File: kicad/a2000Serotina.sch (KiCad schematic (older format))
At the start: 236 parts, among them J1 90121-0766, U1 Teensy++2.0_(C)

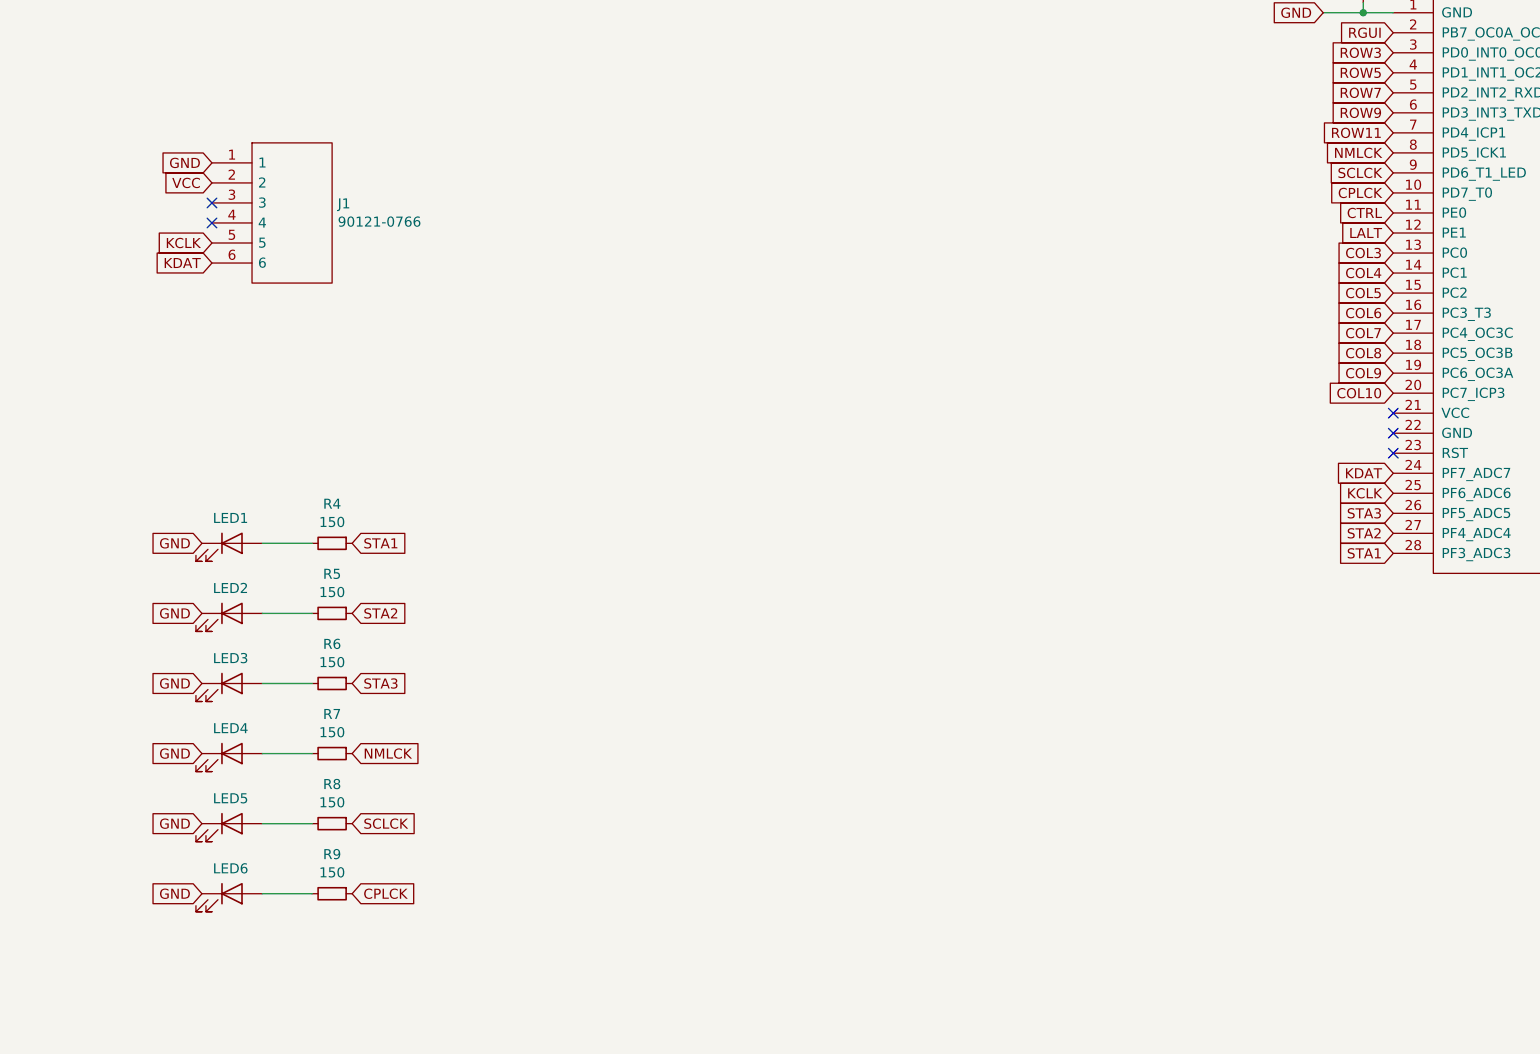
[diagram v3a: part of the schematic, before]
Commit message: Change for V1.4
Now uses a mounting plate from WASD.
1) Adjust dimensions to match WASD PCB
2) Make mounting holes bigger so that PCB sits lower
3) Move resistors so that they are not under plate
4) Move Caps Lock LED to rightmost and move Teensy back to top.
5) J1 moved between Enter + Del
6) Stabilizer holes deleted. Costar Stabilizers now attached to Plate.
7) Minimize hole courtyards to pass Design Rules Check
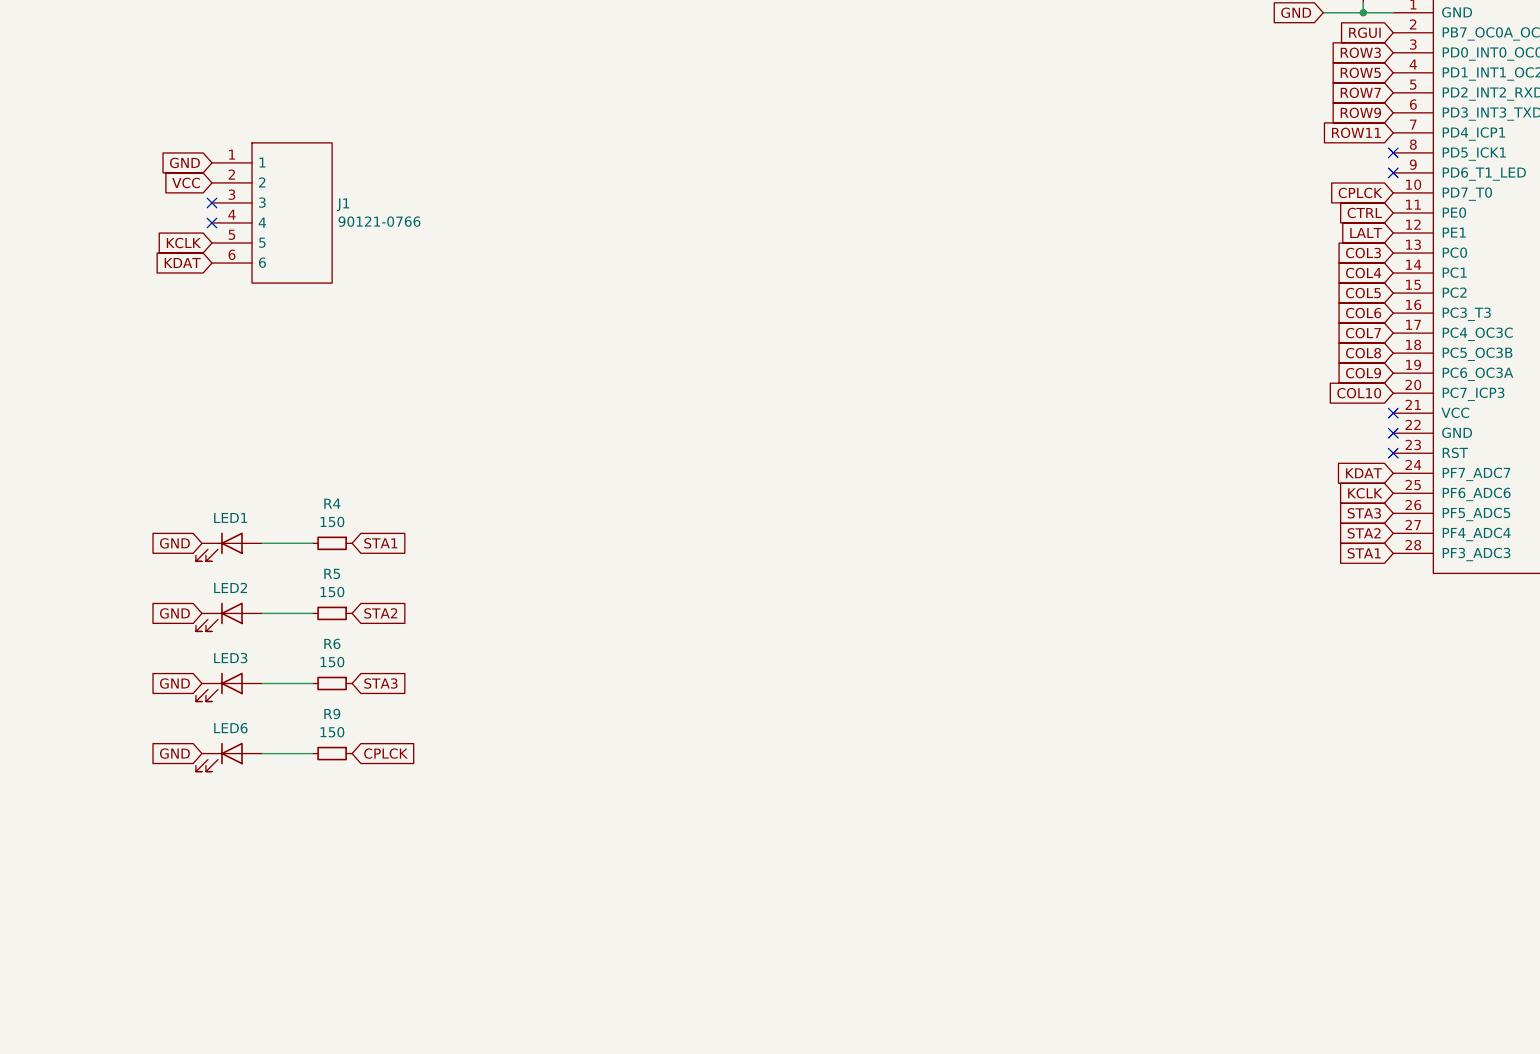
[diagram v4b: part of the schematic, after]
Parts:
- removed LED4, LED5: LED, LED_THT:LED_D3.0mm, symbol Device:LED
- removed R7, R8: 150, Resistor_THT:R_Axial_DIN0207_L6.3mm_D2.5mm_P10.16mm_Horizontal, symbol Device:R_Small
- H1, H2, H3, H4: footprint MountingHole:MountingHole_3.2mm_M3 -> MountingHole:MountingHole_6.4mm_M6
- H5, H6, H7: footprint MountingHole:MountingHole_6.4mm_M6 -> MountingHole:MountingHole_8.4mm_M8
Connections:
- net NMLCK: no longer names the net of U1.8 (PD5_ICK1)
- net SCLCK: no longer names the net of U1.9 (PD6_T1_LED)
- no-connect marks 20 -> 22
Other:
- moved on the sheet: LED6, R9
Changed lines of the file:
@@
 Text GLabel 18300 3800 0    50   Input ~ 0
 COL10
-Text GLabel 18300 2600 0    50   Input ~ 0
-NMLCK
 Text GLabel 18300 2800 0    50   Input ~ 0
 CPLCK
-Text GLabel 18300 2700 0    50   Input ~ 0
-SCLCK
 Text GLabel 18300 4300 0    50   Input ~ 0
 KCLK
@@
 	12650 5250 12900 5250
 $Comp
-L Device:R_Small R7
-U 1 1 60F964C9
-P 13000 5600
-F 0 "R7" V 12804 5600 50  0000 C CNN
-F 1 "150" V 12895 5600 50  0000 C CNN
-F 2 "Resistor_THT:R_Axial_DIN0207_L6.3mm_D2.5mm_P10.16mm_Horizontal" H 13000 5600 50  0001 C CNN
-F 3 "~" H 13000 5600 50  0001 C CNN
-	1    13000 5600
-	0    1    1    0
-$EndComp
-Text GLabel 13100 5600 2    50   Input ~ 0
-NMLCK
-$Comp
-L Device:LED LED4
-U 1 1 60F964D0
-P 12500 5600
-F 0 "LED4" H 12493 5725 50  0000 C CNN
-F 1 "LED" H 12493 5725 50  0001 C CNN
-F 2 "LED_THT:LED_D3.0mm" H 12500 5600 50  0001 C CNN
-F 3 "~" H 12500 5600 50  0001 C CNN
-	1    12500 5600
-	1    0    0    -1
-$EndComp
-Text GLabel 12350 5600 0    50   Input ~ 0
-GND
-Wire Wire Line
-	12650 5600 12900 5600
-$Comp
-L Device:R_Small R8
-U 1 1 60FB4C04
-P 13000 5950
-F 0 "R8" V 12804 5950 50  0000 C CNN
-F 1 "150" V 12895 5950 50  0000 C CNN
-F 2 "Resistor_THT:R_Axial_DIN0207_L6.3mm_D2.5mm_P10.16mm_Horizontal" H 13000 5950 50  0001 C CNN
-F 3 "~" H 13000 5950 50  0001 C CNN
-	1    13000 5950
-	0    1    1    0
-$EndComp
-Text GLabel 13100 5950 2    50   Input ~ 0
-SCLCK
-$Comp
-L Device:LED LED5
-U 1 1 60FB4C0B
-P 12500 5950
-F 0 "LED5" H 12493 6075 50  0000 C CNN
-F 1 "LED" H 12493 6075 50  0001 C CNN
-F 2 "LED_THT:LED_D3.0mm" H 12500 5950 50  0001 C CNN
-F 3 "~" H 12500 5950 50  0001 C CNN
-	1    12500 5950
-	1    0    0    -1
-$EndComp
-Text GLabel 12350 5950 0    50   Input ~ 0
-GND
-Wire Wire Line
-	12650 5950 12900 5950
-$Comp
 L Device:R_Small R10
 U 1 1 610519E9
@@
 F 0 "H1" H 11600 8546 50  0000 L CNN
 F 1 "MountingHole" H 11600 8455 50  0000 L CNN
-F 2 "MountingHole:MountingHole_3.2mm_M3" H 11500 8500 50  0001 C CNN
+F 2 "MountingHole:MountingHole_6.4mm_M6" H 11500 8500 50  0001 C CNN
 F 3 "~" H 11500 8500 50  0001 C CNN
 	1    11500 8500
@@
 F 0 "H2" H 11600 9046 50  0000 L CNN
 F 1 "MountingHole" H 11600 8955 50  0000 L CNN
-F 2 "MountingHole:MountingHole_3.2mm_M3" H 11500 9000 50  0001 C CNN
+F 2 "MountingHole:MountingHole_6.4mm_M6" H 11500 9000 50  0001 C CNN
 F 3 "~" H 11500 9000 50  0001 C CNN
 	1    11500 9000
@@
 F 0 "H3" H 11600 9546 50  0000 L CNN
 F 1 "MountingHole" H 11600 9455 50  0000 L CNN
-F 2 "MountingHole:MountingHole_3.2mm_M3" H 11500 9500 50  0001 C CNN
+F 2 "MountingHole:MountingHole_6.4mm_M6" H 11500 9500 50  0001 C CNN
 F 3 "~" H 11500 9500 50  0001 C CNN
 	1    11500 9500
@@
 F 0 "H4" H 11600 10046 50  0000 L CNN
 F 1 "MountingHole" H 11600 9955 50  0000 L CNN
-F 2 "MountingHole:MountingHole_3.2mm_M3" H 11500 10000 50  0001 C CNN
+F 2 "MountingHole:MountingHole_6.4mm_M6" H 11500 10000 50  0001 C CNN
 F 3 "~" H 11500 10000 50  0001 C CNN
 	1    11500 10000
@@
 F 0 "H5" H 12600 8546 50  0000 L CNN
 F 1 "MountingHole" H 12600 8455 50  0000 L CNN
-F 2 "MountingHole:MountingHole_6.4mm_M6" H 12500 8500 50  0001 C CNN
+F 2 "MountingHole:MountingHole_8.4mm_M8" H 12500 8500 50  0001 C CNN
 F 3 "~" H 12500 8500 50  0001 C CNN
 	1    12500 8500
@@
 F 0 "H6" H 12600 9046 50  0000 L CNN
 F 1 "MountingHole" H 12600 8955 50  0000 L CNN
-F 2 "MountingHole:MountingHole_6.4mm_M6" H 12500 9000 50  0001 C CNN
+F 2 "MountingHole:MountingHole_8.4mm_M8" H 12500 9000 50  0001 C CNN
 F 3 "~" H 12500 9000 50  0001 C CNN
 	1    12500 9000
@@
 F 0 "H7" H 12600 9546 50  0000 L CNN
 F 1 "MountingHole" H 12600 9455 50  0000 L CNN
-F 2 "MountingHole:MountingHole_6.4mm_M6" H 12500 9500 50  0001 C CNN
+F 2 "MountingHole:MountingHole_8.4mm_M8" H 12500 9500 50  0001 C CNN
 F 3 "~" H 12500 9500 50  0001 C CNN
 	1    12500 9500
@@
 Connection ~ 3750 9750
 Wire Wire Line
-	12650 6300 12900 6300
-Text GLabel 12350 6300 0    50   Input ~ 0
+	12650 5600 12900 5600
+Text GLabel 12350 5600 0    50   Input ~ 0
 GND
 $Comp
 L Device:LED LED6
 U 1 1 60FD4854
-P 12500 6300
-F 0 "LED6" H 12493 6425 50  0000 C CNN
-F 1 "LED" H 12493 6425 50  0001 C CNN
-F 2 "LED_THT:LED_D3.0mm" H 12500 6300 50  0001 C CNN
-F 3 "~" H 12500 6300 50  0001 C CNN
-	1    12500 6300
+P 12500 5600
+F 0 "LED6" H 12493 5725 50  0000 C CNN
+F 1 "LED" H 12493 5725 50  0001 C CNN
+F 2 "LED_THT:LED_D3.0mm" H 12500 5600 50  0001 C CNN
+F 3 "~" H 12500 5600 50  0001 C CNN
+	1    12500 5600
 	1    0    0    -1
 $EndComp
-Text GLabel 13100 6300 2    50   Input ~ 0
+Text GLabel 13100 5600 2    50   Input ~ 0
 CPLCK
 $Comp
 L Device:R_Small R9
 U 1 1 60FD484D
-P 13000 6300
-F 0 "R9" V 12804 6300 50  0000 C CNN
-F 1 "150" V 12895 6300 50  0000 C CNN
-F 2 "Resistor_THT:R_Axial_DIN0207_L6.3mm_D2.5mm_P10.16mm_Horizontal" H 13000 6300 50  0001 C CNN
-F 3 "~" H 13000 6300 50  0001 C CNN
-	1    13000 6300
+P 13000 5600
+F 0 "R9" V 12804 5600 50  0000 C CNN
+F 1 "150" V 12895 5600 50  0000 C CNN
+F 2 "Resistor_THT:R_Axial_DIN0207_L6.3mm_D2.5mm_P10.16mm_Horizontal" H 13000 5600 50  0001 C CNN
+F 3 "~" H 13000 5600 50  0001 C CNN
+	1    13000 5600
 	0    1    1    0
 $EndComp
@@
 	1    0    0    -1
 $EndComp
+NoConn ~ 18300 2600
+NoConn ~ 18300 2700
 $EndSCHEMATC

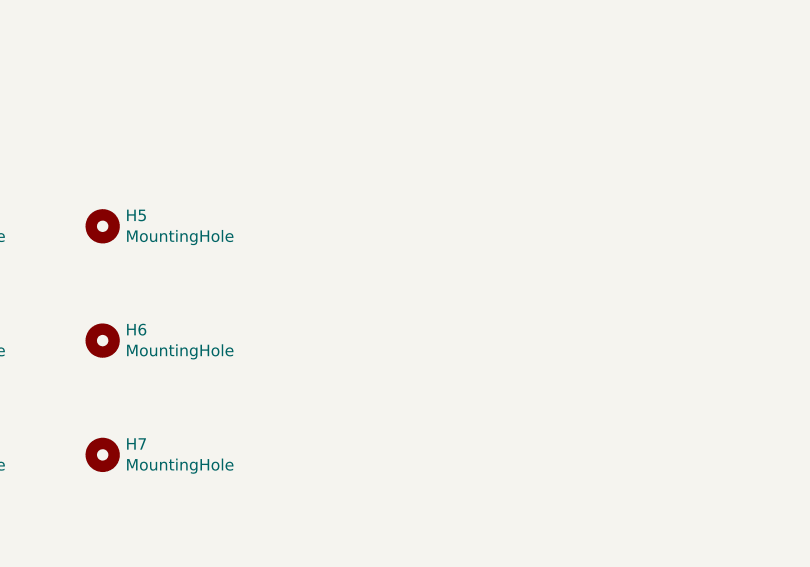
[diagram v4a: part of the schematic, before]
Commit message: Add two additional mounting holes
To match WASD PCB.
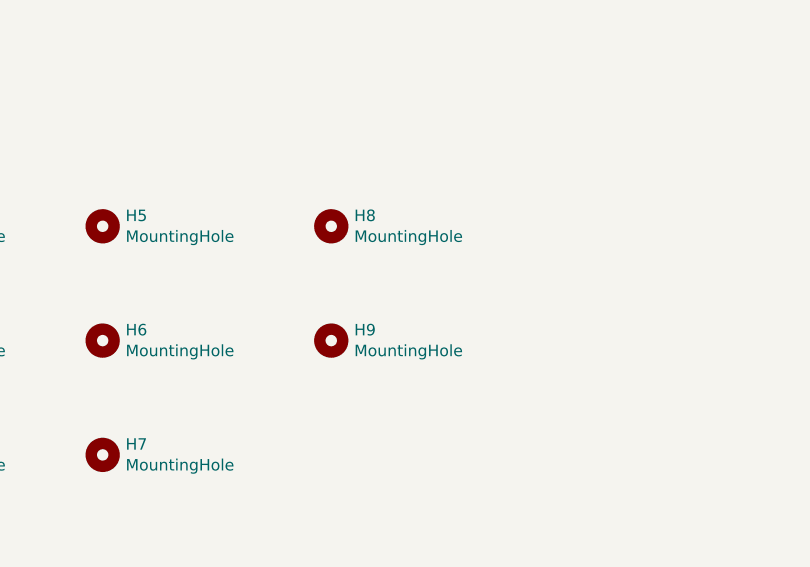
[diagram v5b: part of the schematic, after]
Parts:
- added H8, H9: MountingHole, MountingHole:MountingHole_2.5mm, symbol Mechanical:MountingHole
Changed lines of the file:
@@
 NoConn ~ 18300 2600
 NoConn ~ 18300 2700
+$Comp
+L Mechanical:MountingHole H8
+U 1 1 615DC189
+P 13500 8500
+F 0 "H8" H 13600 8546 50  0000 L CNN
+F 1 "MountingHole" H 13600 8455 50  0000 L CNN
+F 2 "MountingHole:MountingHole_2.5mm" H 13500 8500 50  0001 C CNN
+F 3 "~" H 13500 8500 50  0001 C CNN
+	1    13500 8500
+	1    0    0    -1
+$EndComp
+$Comp
+L Mechanical:MountingHole H9
+U 1 1 615DD58D
+P 13500 9000
+F 0 "H9" H 13600 9046 50  0000 L CNN
+F 1 "MountingHole" H 13600 8955 50  0000 L CNN
+F 2 "MountingHole:MountingHole_2.5mm" H 13500 9000 50  0001 C CNN
+F 3 "~" H 13500 9000 50  0001 C CNN
+	1    13500 9000
+	1    0    0    -1
+$EndComp
 $EndSCHEMATC
